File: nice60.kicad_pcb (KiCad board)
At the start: 2 copper layers, 285 x 94.6 mm, 141 parts, among them J1 USB_C_Receptacle_USB2.0, J2 Conn_01x04_Female, J3 Conn_01x02_Female, SW1 SW_Push, U1 ProMicro, U2 USBLC6-2SC6

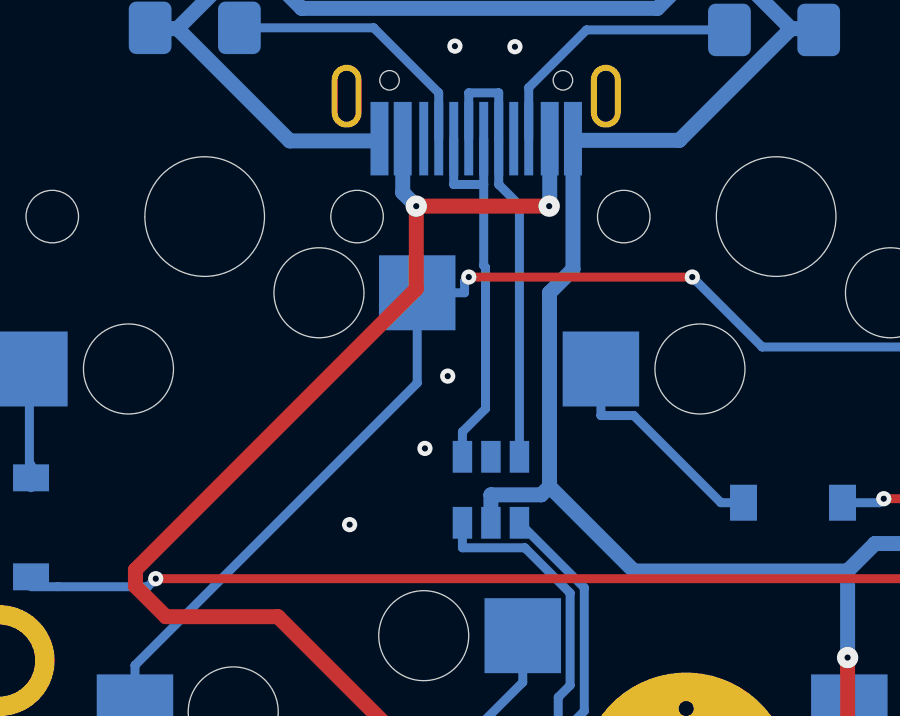
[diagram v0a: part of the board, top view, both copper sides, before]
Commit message: Fix VBUS connection to ESD protection
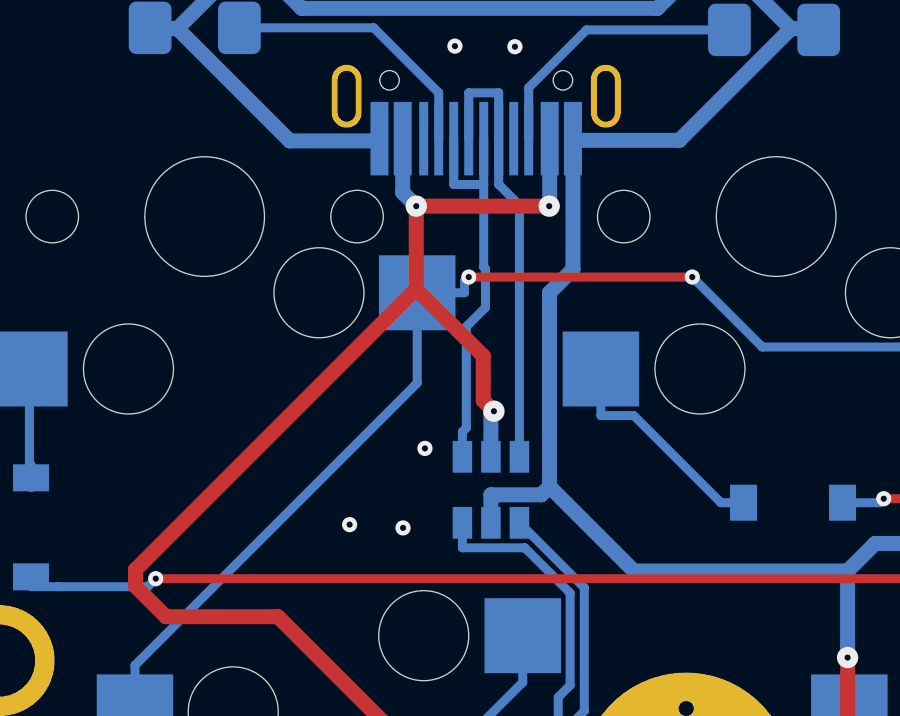
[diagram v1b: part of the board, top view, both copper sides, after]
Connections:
- U2 pad 5: Net-(U2-Pad5) -> VBUS
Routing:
- net VBUS: track 50.8 -> 57.5 mm, vias 2 -> 3

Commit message: Add better JST connector silkscreen
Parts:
- added J3: Conn_01x02_Female, Connector_JST:JST_PH_S2B-PH-K_1x02_P2.00mm_Horizontal, B.Cu at (124.5, 52.7)
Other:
- board text added: "Bat+"
- board text added: "Bat-"
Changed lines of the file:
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@@
   (general
     (thickness 1.6)
-    (drawings 4)
+    (drawings 8)
     (tracks 1668)
     (zones 0)
-    (modules 141)
+    (modules 142)
     (nets 103)
   )
@@
     (add_net VCC)
   )
+  (module Connector_JST:JST_PH_S2B-PH-K_1x02_P2.00mm_Horizontal (layer B.Cu)
+    (at 124.46 52.68 90)
+    (descr "JST PH series connector, S2B-PH-K (http://www.jst-mfg.com/product/pdf/eng/ePH.pdf), generated with kicad-footprint-generator")
+    (tags "connector JST PH top entry")
+    (fp_text reference J3 (at 1 2.55 90) (layer B.SilkS) hide
+      (effects (font (size 1 1) (thickness 0.15)) (justify mirror))
+    )
+    (fp_text value Conn_01x02_Female (at 1 -7.45 90) (layer B.Fab)
+      (effects (font (size 1 1) (thickness 0.15)) (justify mirror))
+    )
+    (fp_line (start -0.86 -0.14) (end -1.14 -0.14) (layer B.SilkS) (width 0.12))
+    (fp_line (start -1.14 -0.14) (end -1.14 1.46) (layer B.SilkS) (width 0.12))
+    (fp_line (start -1.14 1.46) (end -2.06 1.46) (layer B.SilkS) (width 0.12))
+    (fp_line (start -2.06 1.46) (end -2.06 -6.36) (layer B.SilkS) (width 0.12))
+    (fp_line (start -2.06 -6.36) (end 4.06 -6.36) (layer B.SilkS) (width 0.12))
+    (fp_line (start 4.06 -6.36) (end 4.06 1.46) (layer B.SilkS) (width 0.12))
+    (fp_line (start 4.06 1.46) (end 3.14 1.46) (layer B.SilkS) (width 0.12))
+    (fp_line (start 3.14 1.46) (end 3.14 -0.14) (layer B.SilkS) (width 0.12))
+    (fp_line (start 3.14 -0.14) (end 2.86 -0.14) (layer B.SilkS) (width 0.12))
+    (fp_line (start 0.5 -6.36) (end 0.5 -2) (layer B.SilkS) (width 0.12))
+    (fp_line (start 0.5 -2) (end 1.5 -2) (layer B.SilkS) (width 0.12))
+    (fp_line (start 1.5 -2) (end 1.5 -6.36) (layer B.SilkS) (width 0.12))
+    (fp_line (start -2.06 -0.14) (end -1.14 -0.14) (layer B.SilkS) (width 0.12))
+    (fp_line (start 4.06 -0.14) (end 3.14 -0.14) (layer B.SilkS) (width 0.12))
+    (fp_line (start -1.3 -2.5) (end -1.3 -4.1) (layer B.SilkS) (width 0.12))
+    (fp_line (start -1.3 -4.1) (end -0.3 -4.1) (layer B.SilkS) (width 0.12))
+    (fp_line (start -0.3 -4.1) (end -0.3 -2.5) (layer B.SilkS) (width 0.12))
+    (fp_line (start -0.3 -2.5) (end -1.3 -2.5) (layer B.SilkS) (width 0.12))
+    (fp_line (start 3.3 -2.5) (end 3.3 -4.1) (layer B.SilkS) (width 0.12))
+    (fp_line (start 3.3 -4.1) (end 2.3 -4.1) (layer B.SilkS) (width 0.12))
+    (fp_line (start 2.3 -4.1) (end 2.3 -2.5) (layer B.SilkS) (width 0.12))
+    (fp_line (start 2.3 -2.5) (end 3.3 -2.5) (layer B.SilkS) (width 0.12))
+    (fp_line (start -0.3 -4.1) (end -0.3 -6.36) (layer B.SilkS) (width 0.12))
+    (fp_line (start -0.8 -4.1) (end -0.8 -6.36) (layer B.SilkS) (width 0.12))
+    (fp_line (start -2.45 1.85) (end -2.45 -6.75) (layer B.CrtYd) (width 0.05))
+    (fp_line (start -2.45 -6.75) (end 4.45 -6.75) (layer B.CrtYd) (width 0.05))
+    (fp_line (start 4.45 -6.75) (end 4.45 1.85) (layer B.CrtYd) (width 0.05))
+    (fp_line (start 4.45 1.85) (end -2.45 1.85) (layer B.CrtYd) (width 0.05))
+    (fp_line (start -1.25 -0.25) (end -1.25 1.35) (layer B.Fab) (width 0.1))
+    (fp_line (start -1.25 1.35) (end -1.95 1.35) (layer B.Fab) (width 0.1))
+    (fp_line (start -1.95 1.35) (end -1.95 -6.25) (layer B.Fab) (width 0.1))
+    (fp_line (start -1.95 -6.25) (end 3.95 -6.25) (layer B.Fab) (width 0.1))
+    (fp_line (start 3.95 -6.25) (end 3.95 1.35) (layer B.Fab) (width 0.1))
+    (fp_line (start 3.95 1.35) (end 3.25 1.35) (layer B.Fab) (width 0.1))
+    (fp_line (start 3.25 1.35) (end 3.25 -0.25) (layer B.Fab) (width 0.1))
+    (fp_line (start 3.25 -0.25) (end -1.25 -0.25) (layer B.Fab) (width 0.1))
+    (fp_line (start -0.86 -0.14) (end -0.86 1.075) (layer B.SilkS) (width 0.12))
+    (fp_line (start 0 -0.875) (end -0.5 -1.375) (layer B.Fab) (width 0.1))
+    (fp_line (start -0.5 -1.375) (end 0.5 -1.375) (layer B.Fab) (width 0.1))
+    (fp_line (start 0.5 -1.375) (end 0 -0.875) (layer B.Fab) (width 0.1))
+    (fp_text user %R (at 1 -2.5 90) (layer B.Fab)
+      (effects (font (size 1 1) (thickness 0.15)) (justify mirror))
+    )
+    (pad 1 thru_hole roundrect (at 0 0 90) (size 1.2 1.75) (drill 0.75) (layers *.Cu *.Mask) (roundrect_rratio 0.208333))
+    (pad 2 thru_hole oval (at 2 0 90) (size 1.2 1.75) (drill 0.75) (layers *.Cu *.Mask))
+    (model ${KISYS3DMOD}/Connector_JST.3dshapes/JST_PH_S2B-PH-K_1x02_P2.00mm_Horizontal.wrl
+      (at (xyz 0 0 0))
+      (scale (xyz 1 1 1))
+      (rotate (xyz 0 0 0))
+    )
+  )
   (module amtra5_outline:60_Outline-Modded-Type-C (layer F.Cu)
     (at 158.228 62.292)
@@
     (descr "JST PH series connector, S2B-PH-K (http://www.jst-mfg.com/product/pdf/eng/ePH.pdf), generated with kicad-footprint-generator")
     (tags "connector JST PH top entry")
-    (fp_text reference J3 (at 1 2.55 90) (layer B.SilkS)
+    (fp_text reference J3 (at 5.18 -0.01 90) (layer B.SilkS)
       (effects (font (size 1 1) (thickness 0.15)) (justify mirror))
     )
@@
     )
   )
+  (gr_text Bat- (at 116.08 53.23) (layer B.SilkS)
+    (effects (font (size 1 1) (thickness 0.15)) (justify mirror))
+  )
+  (gr_text Bat+ (at 116.09 50.25) (layer B.SilkS)
+    (effects (font (size 1 1) (thickness 0.15)) (justify mirror))
+  )
+  (gr_text Bat- (at 132.9 52.85) (layer B.SilkS)
+    (effects (font (size 1 1) (thickness 0.15)) (justify mirror))
+  )
+  (gr_text Bat+ (at 132.91 49.87) (layer B.SilkS)
+    (effects (font (size 1 1) (thickness 0.15)) (justify mirror))
+  )
   (gr_line (start 33.87 65.58) (end 30.17 65.58) (layer Edge.Cuts) (width 0.05))
   (gr_line (start 33.87 68.88) (end 30.17 68.88) (layer Edge.Cuts) (width 0.05))
@@
   (via (at 131.3455 66.9079) (size 0.508) (layers F.Cu B.Cu) (net 79))
   (segment (start 98.755 78.802) (end 98.755 77.2493) (width 0.3) (layer B.Cu) (net 79) (status 10))
-  (segment (start 139.597 48.4031) (end 141.617 46.3831) (width 0.3) (layer B.Cu) (net 79))
-  (segment (start 124.9175 48.4031) (end 139.597 48.4031) (width 0.3) (layer B.Cu) (net 79))
-  (segment (start 123.2461 50.0745) (end 124.9175 48.4031) (width 0.3) (layer B.Cu) (net 79))
-  (segment (start 123.2461 51.257) (end 123.2461 50.0745) (width 0.3) (layer B.Cu) (net 79))
-  (segment (start 123.7468 51.7577) (end 123.2461 51.257) (width 0.3) (layer B.Cu) (net 79))
-  (segment (start 125.0944 51.7577) (end 123.7468 51.7577) (width 0.3) (layer B.Cu) (net 79))
-  (segment (start 127.33 53.9933) (end 125.0944 51.7577) (width 0.3) (layer B.Cu) (net 79))
-  (segment (start 127.33 59.752) (end 127.33 53.9933) (width 0.3) (layer B.Cu) (net 79) (status 10))
   (segment (start 141.617 46.3831) (end 141.617 40.702) (width 0.3) (layer B.Cu) (net 79) (status 20))
   (segment (start 139.236 97.852) (end 139.236 96.2993) (width 0.3) (layer B.Cu) (net 79) (status 10))
@@
   (segment (start 173.4362 102.1562) (end 154.8548 102.1562) (width 0.3) (layer B.Cu) (net 79))
   (segment (start 176.14 104.86) (end 173.4362 102.1562) (width 0.3) (layer B.Cu) (net 79) (status 10))
+  (segment (start 139.597 48.4031) (end 141.617 46.3831) (width 0.3) (layer B.Cu) (net 79))
+  (segment (start 123.2461 50.0745) (end 124.9175 48.4031) (width 0.3) (layer B.Cu) (net 79))
+  (segment (start 124.9175 48.4031) (end 139.597 48.4031) (width 0.3) (layer B.Cu) (net 79))
+  (segment (start 127.33 53.793772) (end 125.293928 51.7577) (width 0.3) (layer B.Cu) (net 79))
+  (segment (start 127.33 59.752) (end 127.33 53.793772) (width 0.3) (layer B.Cu) (net 79))
+  (segment (start 125.293928 51.7577) (end 123.7468 51.7577) (width 0.3) (layer B.Cu) (net 79))
+  (segment (start 123.2461 51.257) (end 123.2461 50.0745) (width 0.3) (layer B.Cu) (net 79))
+  (segment (start 123.7468 51.7577) (end 123.2461 51.257) (width 0.3) (layer B.Cu) (net 79))
   (segment (start 208.293 21.652) (end 208.293 20.0993) (width 0.3) (layer B.Cu) (net 80) (status 10))
   (segment (start 205.4779 17.2842) (end 208.293 20.0993) (width 0.3) (layer B.Cu) (net 80))
